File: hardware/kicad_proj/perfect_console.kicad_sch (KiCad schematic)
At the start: 68 parts, among them J1 R_Out, J10 PWR_OUT_Pins, J11 GPIO5-7, J12 USB_Out, J13 I2C, J14 ESP_UART, J15 CH_Flash, J16 CH_UART, J17 Micro_SD_Card, J18 GPIO41, J2 Jack_3.5, J3 L_Out, J4 USB, J5 TP4056_WO_Protect, J6 Bat, J7 PWR_Btn, J8 BTN_Pins, J9 PTT_Btn, Q1 NMOS, Q2 NMOS, Q3 NMOS, Q4 NMOS, Q5 NMOS, Q6 NMOS, SW1 Reset, SW2 Boot, U1 ESP32-S3-WROOM, U2 Display, U3 PCM5102, U4 PAM8403, U5 CH32V006E8R6, U6 USBLC6-2SC6, U7 DC-DC, U8 LoRa, U9 Mic

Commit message: Допрацювання плати
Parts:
- added C12, C13, C15, C16: 10uF, Capacitor_SMD:C_1206_3216Metric, symbol Device:C_Small
- added C14: 0.1uF, Capacitor_SMD:C_1206_3216Metric, symbol Device:C_Small
- U1: value ESP32-S3-WROOM -> ESP32-S3-WROOM1
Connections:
- net +3V3: no longer U8.6 (VBUS)
- net GND1: now also C15.1, C16.1
- net at Q3.3 (D), U8.7 (GND): now also C12.2, C13.2, C14.2
- net 4V2 renamed +4V2
- net +4V2: now also U8.6 (VBUS), C12.1, C13.1, C14.1, C15.2, C16.2
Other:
- moved on the sheet: C5, Q3, Q5, Q6, R10, R13, R14, R15, R16, R17, R18, R9

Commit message: Допрацювання схеми
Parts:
- removed C2: 0.1uF, Capacitor_SMD:C_1206_3216Metric, symbol Device:C_Small
- removed R5: 10K, Resistor_SMD:R_1206_3216Metric_Pad1.30x1.75mm_HandSolder, symbol Device:R_Small
- added C14: 1uF, Capacitor_SMD:C_1206_3216Metric, symbol Device:C_Small
- added R22: 10K, Resistor_SMD:R_1206_3216Metric_Pad1.30x1.75mm_HandSolder, symbol Device:R_Small
- renumbered C9 to C1, C4 to C11, C5 to C12, C6 to C13, C7 to C15, C8 to C16, C1 to C2, C15 to C3, C16 to C4, C3 to C5, C12 to C6, C13 to C7, C14 to C8, C11 to C9, J18 to J15, J15 to J17, J17 to J18, R11 to R10, R12 to R11, R13 to R12, R14 to R13, R15 to R14, R16 to R15, R17 to R16, R18 to R17, R19 to R18, R20 to R19, R21 to R20, R22 to R21, R6 to R5, R7 to R6, R8 to R7, R9 to R8, R10 to R9, U8 to U6, U6 to U7, U9 to U8, U7 to U9
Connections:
- net +3V3: now also R22.1
- net CH_RESET: now also C14.1, R22.2
- net GND: now also C14.2
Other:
- moved on the sheet: C5, R6, R7

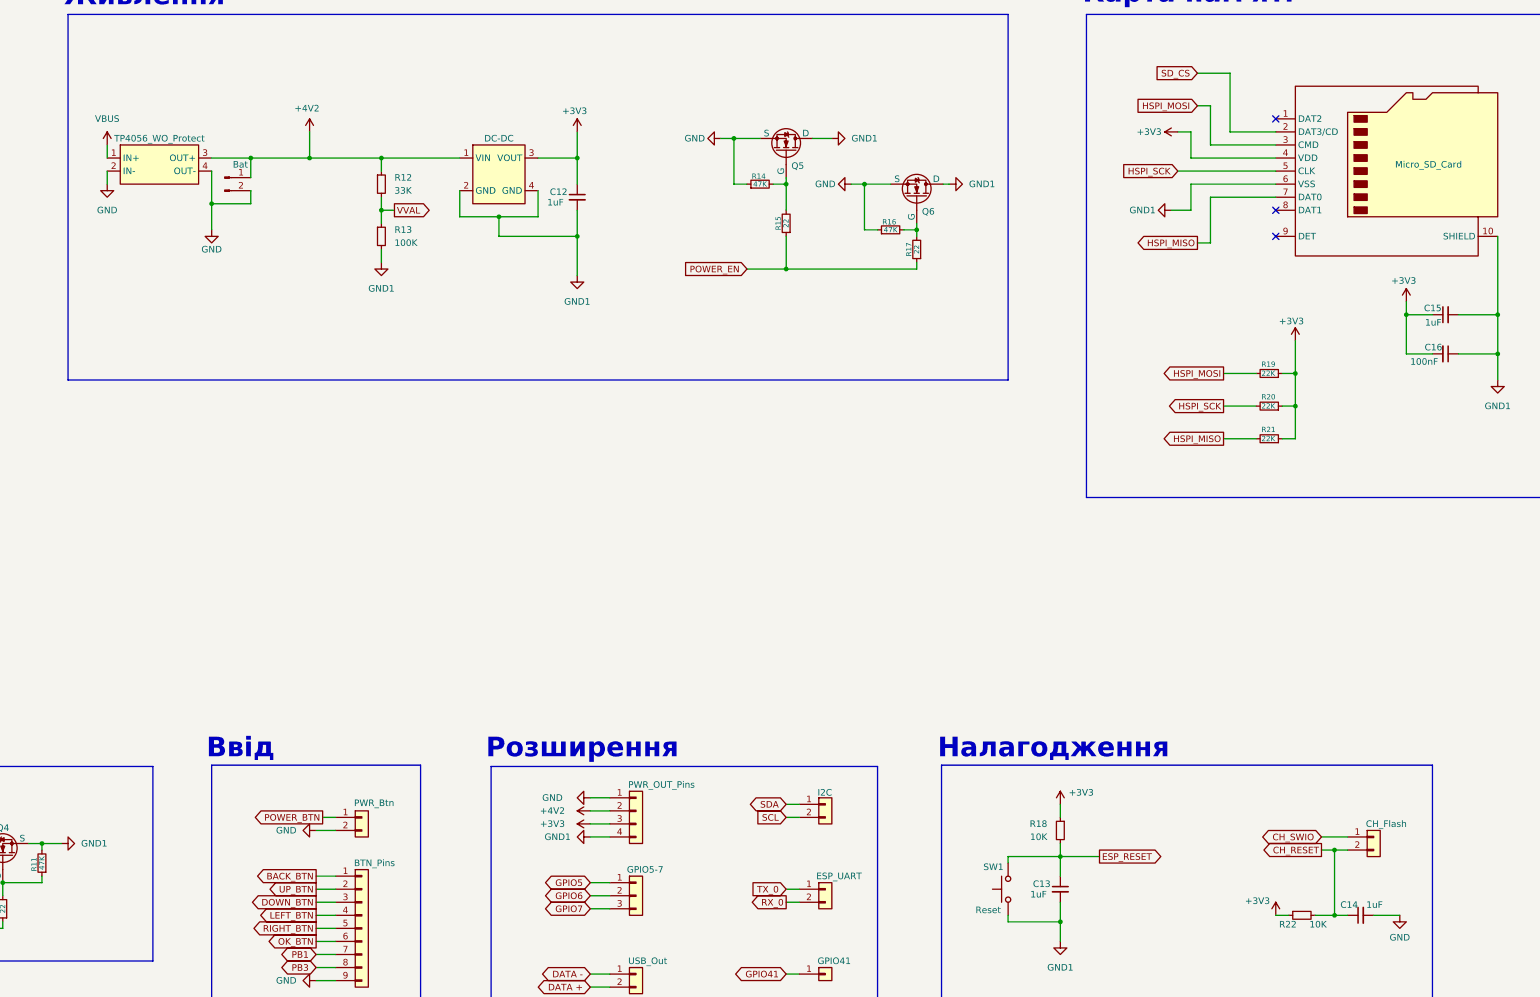
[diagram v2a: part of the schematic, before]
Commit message: Покращення схеми
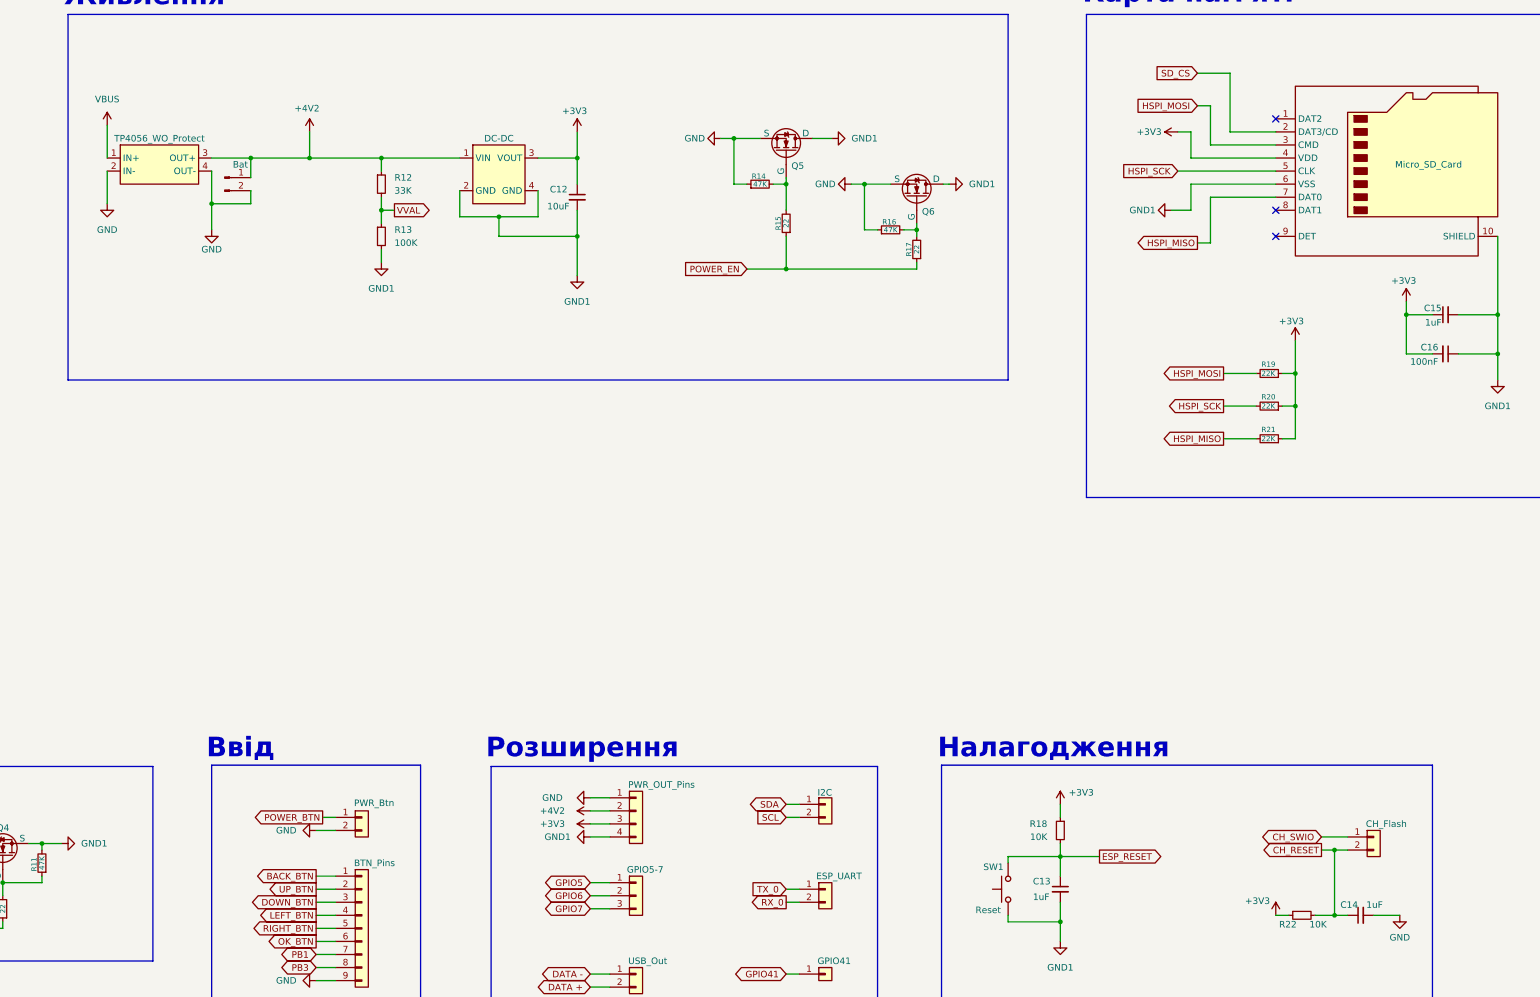
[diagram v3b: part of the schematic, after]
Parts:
- C12: value 1uF -> 10uF
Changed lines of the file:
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@@
 	(wire
 		(pts
-			(xy 379.73 59.69) (xy 379.73 62.23)
+			(xy 379.73 59.69) (xy 379.73 66.04)
 		)
 		(stroke
@@
 	(wire
 		(pts
-			(xy 379.73 54.61) (xy 379.73 57.15)
+			(xy 379.73 50.8) (xy 379.73 57.15)
 		)
 		(stroke
@@
 		(dnp no)
 		(property "Reference" "C16"
-			(at 636.016 93.98 90)
+			(at 635.254 93.98 90)
 			(effects
 				(font
@@
 	(symbol
 		(lib_id "power:GND")
-		(at 379.73 62.23 0)
+		(at 379.73 66.04 0)
 		(mirror y)
 		(unit 1)
@@
 		(fields_autoplaced yes)
 		(property "Reference" "#PWR31"
-			(at 379.73 68.58 0)
+			(at 379.73 72.39 0)
 			(effects
 				(font
@@
 		)
 		(property "Value" "GND"
-			(at 379.73 67.31 0)
+			(at 379.73 71.12 0)
 			(effects
 				(font
@@
 		)
 		(property "Footprint" ""
-			(at 379.73 62.23 0)
+			(at 379.73 66.04 0)
 			(effects
 				(font
@@
 		)
 		(property "Datasheet" ""
-			(at 379.73 62.23 0)
+			(at 379.73 66.04 0)
 			(effects
 				(font
@@
 		)
 		(property "Description" "Power symbol creates a global label with name \"GND\" , ground"
-			(at 379.73 62.23 0)
+			(at 379.73 66.04 0)
 			(effects
 				(font
@@
 	(symbol
 		(lib_id "power:VBUS")
-		(at 379.73 54.61 0)
+		(at 379.73 50.8 0)
 		(mirror y)
 		(unit 1)
@@
 		(fields_autoplaced yes)
 		(property "Reference" "#PWR30"
-			(at 379.73 58.42 0)
+			(at 379.73 54.61 0)
 			(effects
 				(font
@@
 		)
 		(property "Value" "VBUS"
-			(at 379.73 49.53 0)
+			(at 379.73 45.72 0)
 			(effects
 				(font
@@
 		)
 		(property "Footprint" ""
-			(at 379.73 54.61 0)
+			(at 379.73 50.8 0)
 			(effects
 				(font
@@
 		)
 		(property "Datasheet" ""
-			(at 379.73 54.61 0)
+			(at 379.73 50.8 0)
 			(effects
 				(font
@@
 		)
 		(property "Description" "Power symbol creates a global label with name \"VBUS\""
-			(at 379.73 54.61 0)
+			(at 379.73 50.8 0)
 			(effects
 				(font
@@
 		(dnp no)
 		(property "Reference" "C12"
-			(at 465.836 63.754 0)
+			(at 465.836 63.246 0)
 			(effects
 				(font
@@
 			)
 		)
-		(property "Value" "1uF"
-			(at 465.328 65.786 0)
+		(property "Value" "10uF"
+			(at 465.328 66.548 0)
 			(effects
 				(font
@@
 		(dnp no)
 		(property "Reference" "C13"
-			(at 559.816 198.374 0)
+			(at 559.816 197.866 0)
 			(effects
 				(font
@@
 		)
 		(property "Value" "1uF"
-			(at 559.308 200.406 0)
+			(at 559.816 200.914 0)
 			(effects
 				(font

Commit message: Доопрацювання схеми
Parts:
- removed C14: 1uF, Capacitor_SMD:C_1206_3216Metric, symbol Device:C_Small
- removed R22: 10K, Resistor_SMD:R_1206_3216Metric_Pad1.30x1.75mm_HandSolder, symbol Device:R_Small
